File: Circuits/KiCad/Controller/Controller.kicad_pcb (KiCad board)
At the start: 2 copper layers, 175.3 x 109.2 mm, 44 parts, among them J1 Conn_01x15_Male, J2 Conn_01x24_Male, J3 Conn_01x24_Male, U1 74x08, U10 W29C040, U11 74x138, U12 74x377, U13 74x377, U14 74x377, U15 74x377, U16 74x377, U17 74x377, U18 74x04, U19 74x04, U2 74x08, U20 74x32, U21 74x04, U22 74x04, U3 74x04, U4 74x27, U5 74x02, U6 74x161, U7 74x161, U8 74x161, U9 74x74, Y1 8 MHz (max. 10 MHz)

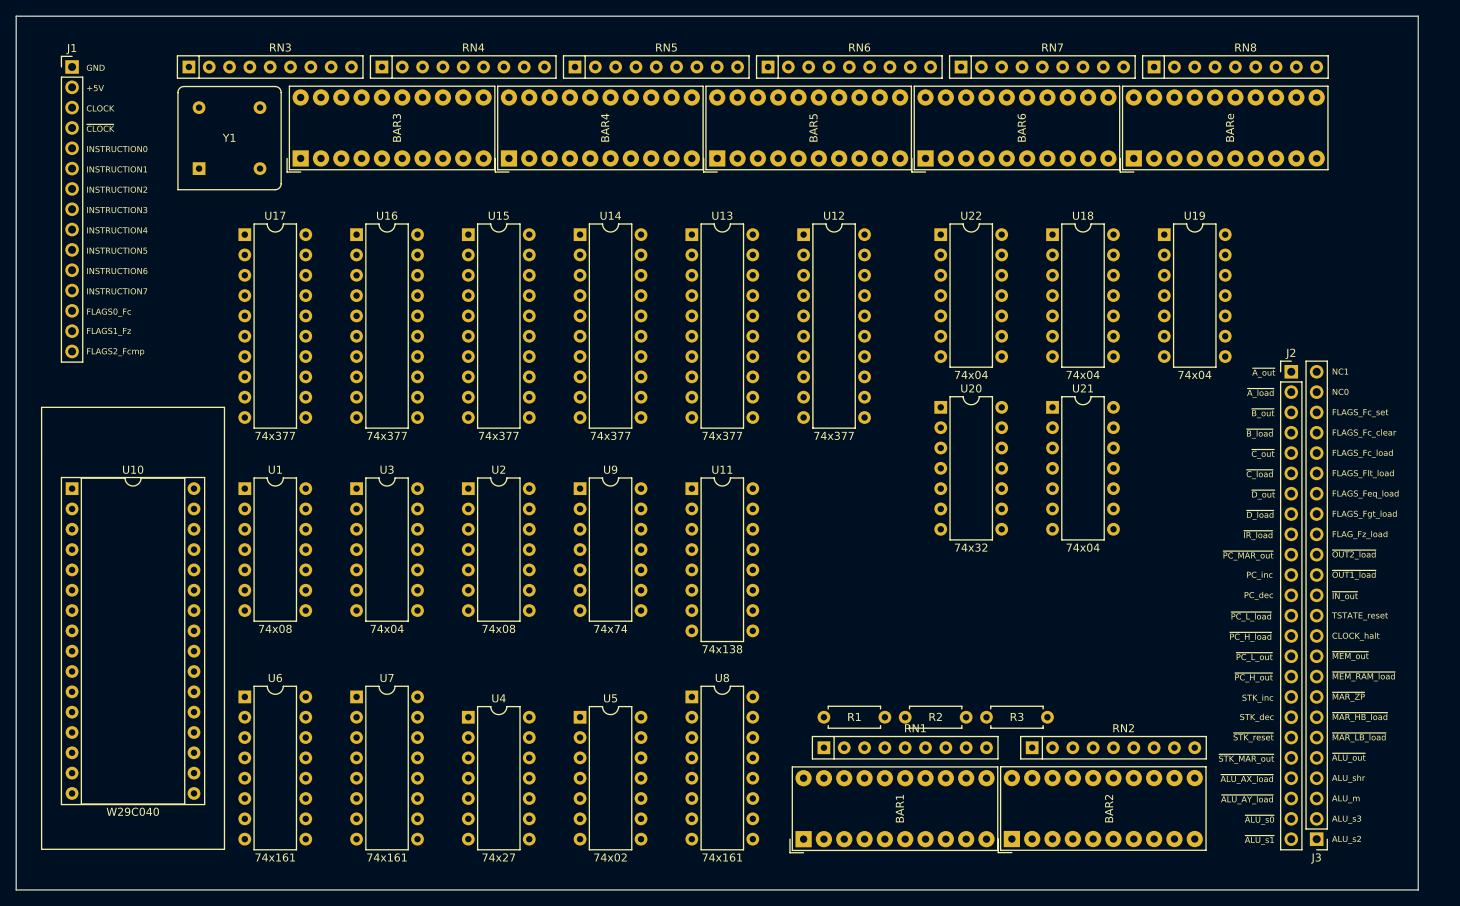
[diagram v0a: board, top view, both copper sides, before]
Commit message: Main board PCB layed out
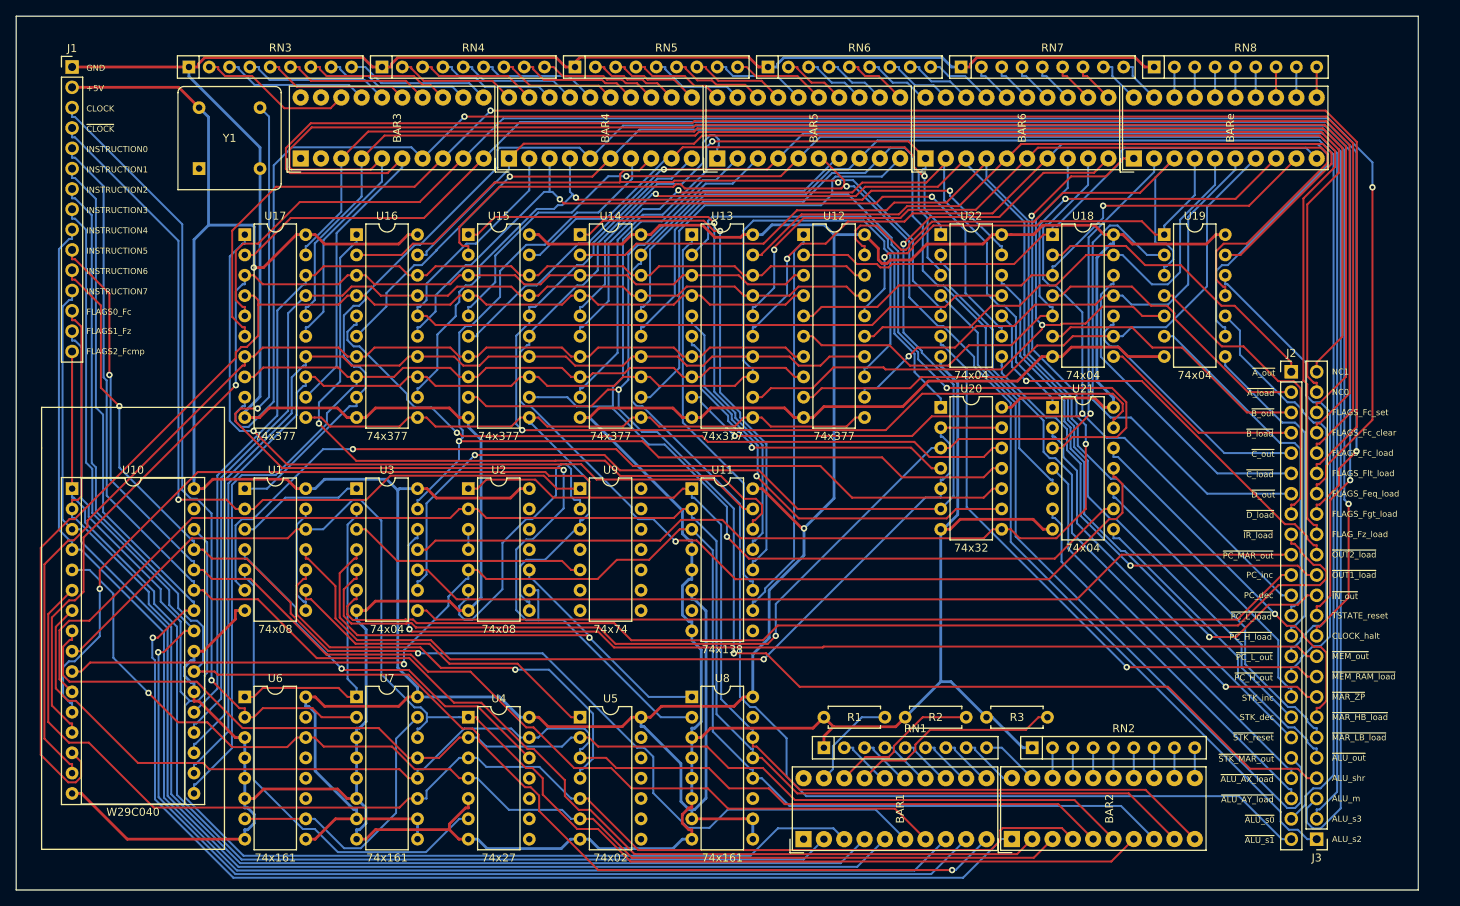
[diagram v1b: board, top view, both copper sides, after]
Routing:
- net GND: track 0.00 -> 672.3 mm
- net +5V: track 0.00 -> 527.6 mm, vias 0 -> 2
- net TSTATE_reset: track 0.00 -> 231.3 mm, vias 0 -> 1
- net FLAGS_Fc_clear: track 0.00 -> 226.5 mm
- net FLAGS_Fc_load: track 0.00 -> 220.4 mm, vias 0 -> 1
- net BANK0: track 0.00 -> 215.0 mm, vias 0 -> 1
- net ALU_m: track 0.00 -> 211.9 mm, vias 0 -> 1
- net FLAGS_Fc_set: track 0.00 -> 210.3 mm
- net FLAGS_Flt_load: track 0.00 -> 206.2 mm, vias 0 -> 1
- net ALU_s3: track 0.00 -> 205.8 mm, vias 0 -> 1
- net FLAGS_Feq_load: track 0.00 -> 204.4 mm, vias 0 -> 1
- net INSTRUCTION1: track 0.00 -> 202.0 mm, vias 0 -> 1
- net CLOCK_halt: track 0.00 -> 199.1 mm, vias 0 -> 2
- net FLAGS_Fgt_load: track 0.00 -> 194.9 mm, vias 0 -> 1
- net INSTRUCTION3: track 0.00 -> 189.7 mm, vias 0 -> 1
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
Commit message: Removed old (obsolete) circuit schematics
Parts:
- moved J3 1.91 mm to (184.8, 129.5)
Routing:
- net GND: track 672.3 -> 0.00 mm
- net +5V: track 527.6 -> 0.00 mm, vias 2 -> 0
- net TSTATE_reset: track 231.3 -> 0.00 mm, vias 1 -> 0
- net FLAGS_Fc_clear: track 226.5 -> 0.00 mm
- net FLAGS_Fc_load: track 220.4 -> 0.00 mm, vias 1 -> 0
- net BANK0: track 215.0 -> 0.00 mm, vias 1 -> 0
- net ALU_m: track 211.9 -> 0.00 mm, vias 1 -> 0
- net FLAGS_Fc_set: track 210.3 -> 0.00 mm
- net FLAGS_Flt_load: track 206.2 -> 0.00 mm, vias 1 -> 0
- net ALU_s3: track 205.8 -> 0.00 mm, vias 1 -> 0
- net FLAGS_Feq_load: track 204.4 -> 0.00 mm, vias 1 -> 0
- net INSTRUCTION1: track 202.0 -> 0.00 mm, vias 1 -> 0
- net CLOCK_halt: track 199.1 -> 0.00 mm, vias 2 -> 0
- net FLAGS_Fgt_load: track 194.9 -> 0.00 mm, vias 1 -> 0
- net INSTRUCTION3: track 189.7 -> 0.00 mm, vias 1 -> 0
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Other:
- board size 175.3 x 109.2 mm -> 177.2 x 109.2 mm

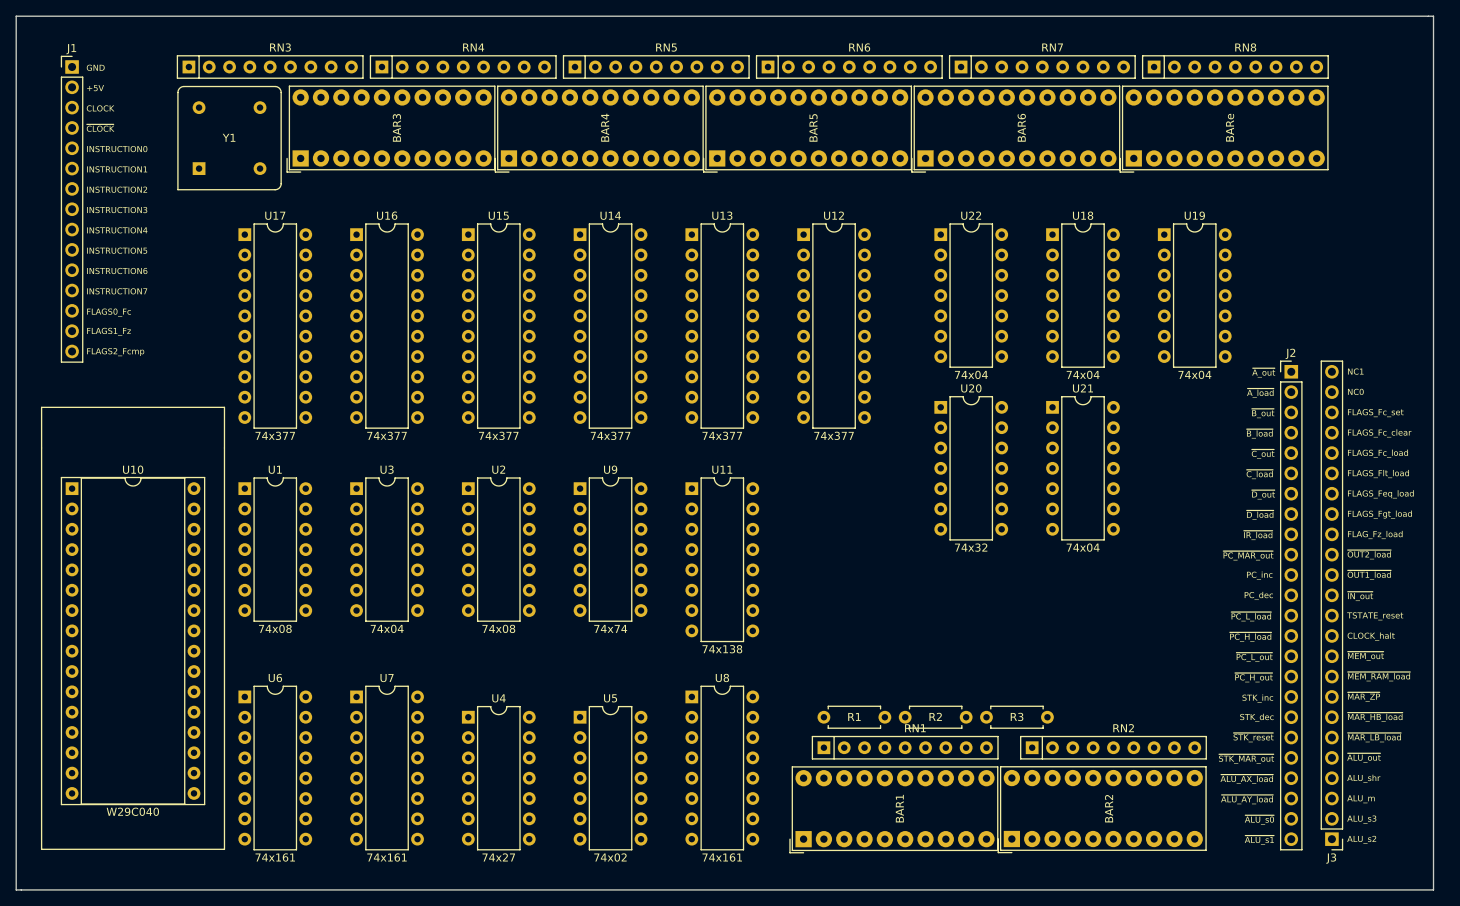
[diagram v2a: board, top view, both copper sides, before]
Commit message: Rerouted Controller and Main board (needs work)
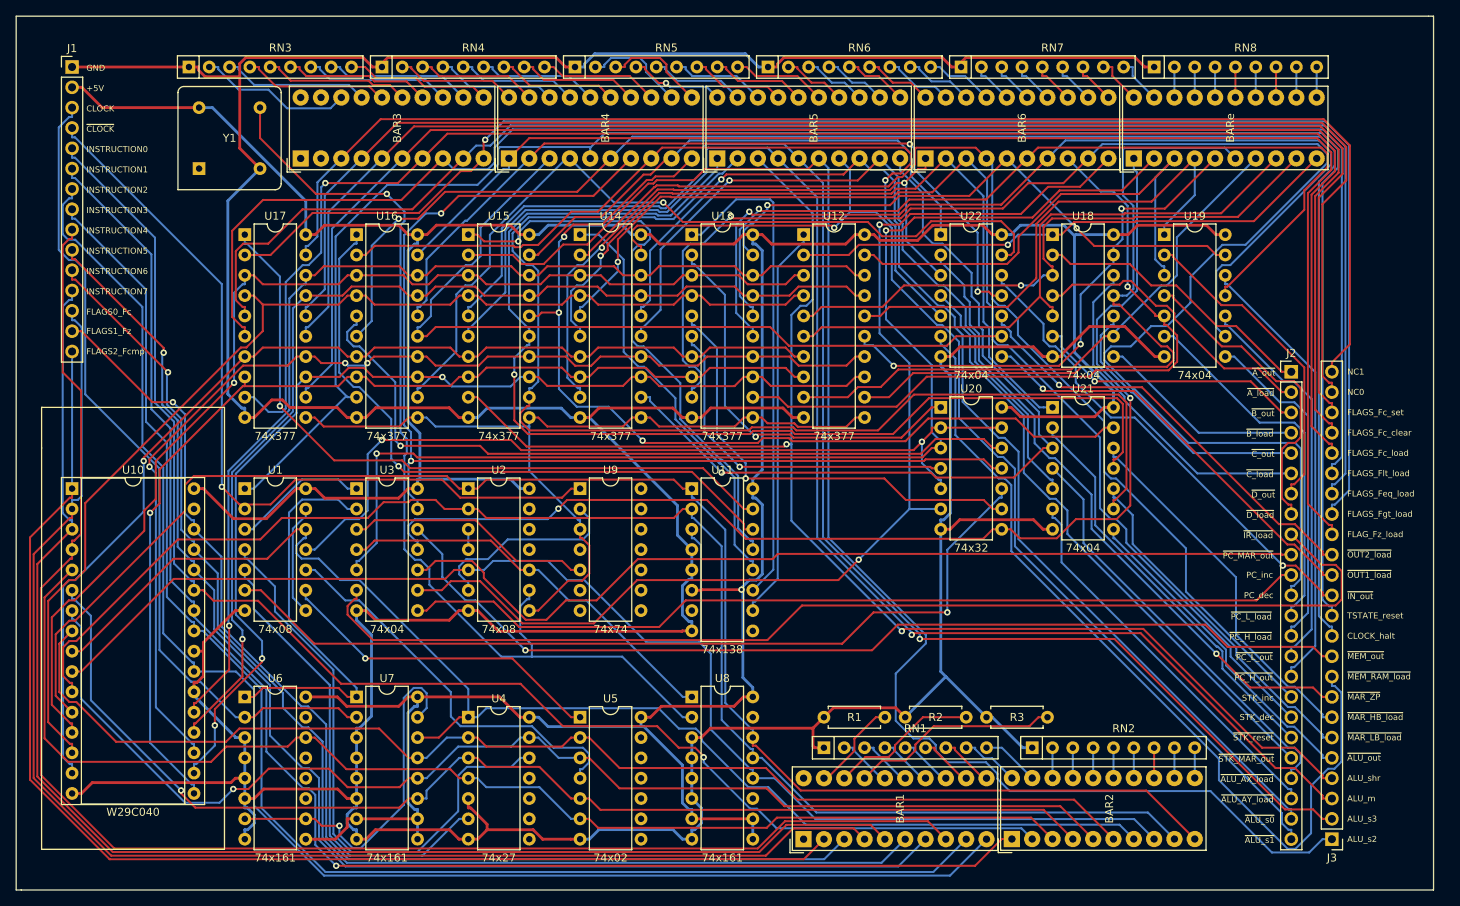
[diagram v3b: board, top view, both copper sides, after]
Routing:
- net GND: track 0.00 -> 658.4 mm
- net +5V: track 0.00 -> 469.1 mm, vias 0 -> 1
- net TSTATE_reset: track 0.00 -> 233.2 mm
- net FLAGS_Fc_load: track 0.00 -> 206.6 mm, vias 0 -> 1
- net FLAGS_Flt_load: track 0.00 -> 202.6 mm
- net CLOCK_halt: track 0.00 -> 201.2 mm, vias 0 -> 1
- net FLAGS_Feq_load: track 0.00 -> 199.4 mm
- net BANK0: track 0.00 -> 197.4 mm
- net PC_dec: track 0.00 -> 196.9 mm, vias 0 -> 1
- net FLAGS_Fgt_load: track 0.00 -> 194.6 mm, vias 0 -> 1
- net FLAGS_Fc_clear: track 0.00 -> 192.2 mm
- net INSTRUCTION4: track 0.00 -> 191.5 mm
- net ALU_s2: track 0.00 -> 190.0 mm
- net INSTRUCTION2: track 0.00 -> 188.5 mm
- net INSTRUCTION1: track 0.00 -> 187.5 mm, vias 0 -> 1
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
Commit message: Finished Controller PCB
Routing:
- net GND: track 658.4 -> 277.8 mm
- net +5V: track 469.1 -> 467.6 mm
- net FLAGS0_Fc: track 172.0 -> 171.2 mm
- net Net-(BAR7-Pad19): track 6.05 -> 5.39 mm
- net Net-(BAR7-Pad20): track 6.05 -> 5.39 mm
- net BANK0: track 197.4 -> 197.9 mm
- net INSTRUCTION4: track 191.5 -> 191.0 mm
- added copper zone on B.Cu, net GND
